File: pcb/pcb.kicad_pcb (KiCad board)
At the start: 2 copper layers, 46 x 58 mm, 39 parts, among them J1 USB_C_Receptacle_USB2.0_14P, J3 LCD DATA, J4 LCD CTRL, J5 MOISTURE, J6 HC-05, J7 DEBUG, J9 USART3 TX, SW1 PWR SWITCH, U1 TLV62569DBV, U2 STM32F446RETx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

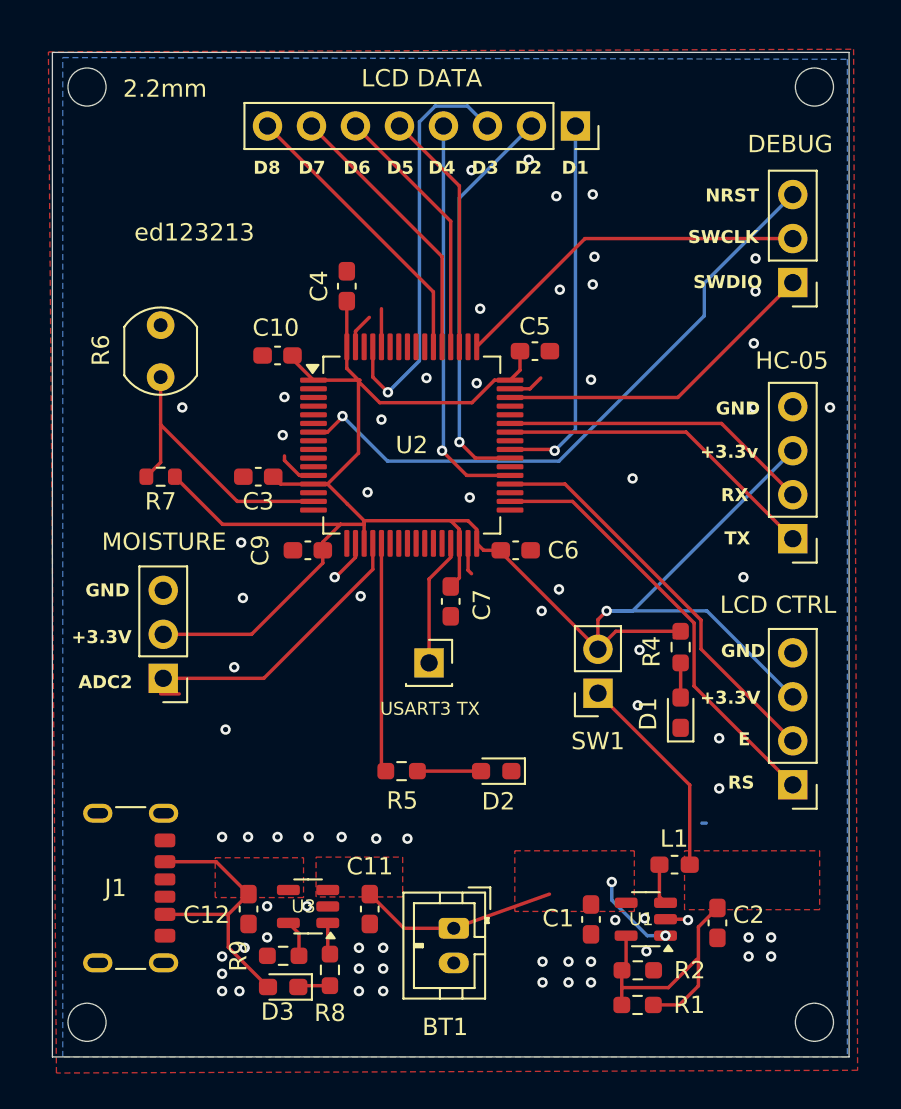
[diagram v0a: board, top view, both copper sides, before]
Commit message: add vcap capacitor and widen traces
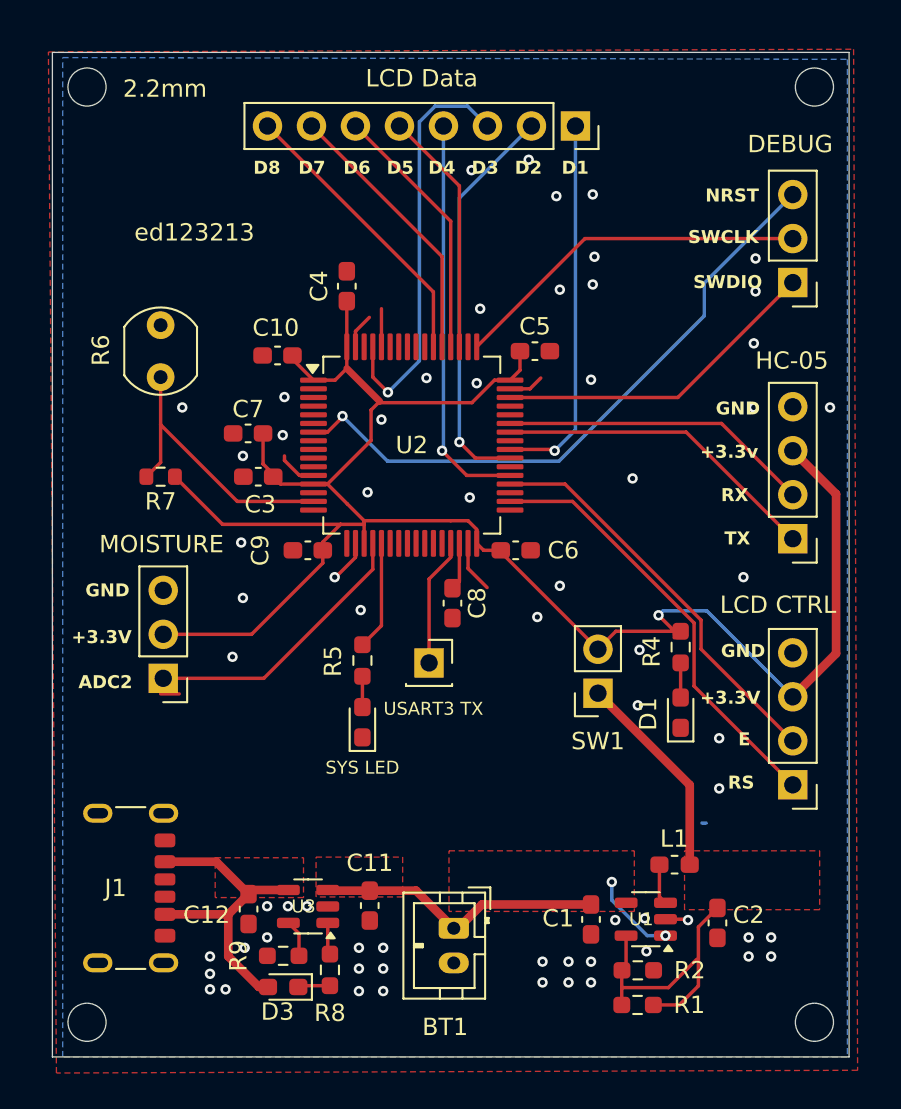
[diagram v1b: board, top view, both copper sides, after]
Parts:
- added C8: 4.7uF, Capacitor_SMD:C_0603_1608Metric_Pad1.08x0.95mm_HandSolder, F.Cu at (88.1, 72.3)
- J3: value LCD DATA -> LCD Data
- moved C7 15.2 mm to (76.3, 62.5), turned to 180 degrees
- moved D2 8.23 mm to (82.9, 79.2), turned to 90 degrees
- moved R5 6.78 mm to (82.9, 75.6), turned to 90 degrees
- moved C11 0.20 mm to (83.3, 89.8)
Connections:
- U2 pad 30: +3.3V -> Net-(U2-VCAP_1)
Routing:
- net +3.7V: track 10.7 -> 21.7 mm
- net SYS LED: track 13.3 -> 6.31 mm
- net +3.3V: track 147.5 -> 142.9 mm
- net Net-(U2-VCAP_1): track 0.00 -> 2.75 mm
- net +5V: track 16.1 -> 18.8 mm
- net Net-(D2-A): track 3.67 -> 1.77 mm
- net GND: track 14.8 -> 15.8 mm, vias 71 -> 65

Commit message: increase board outline
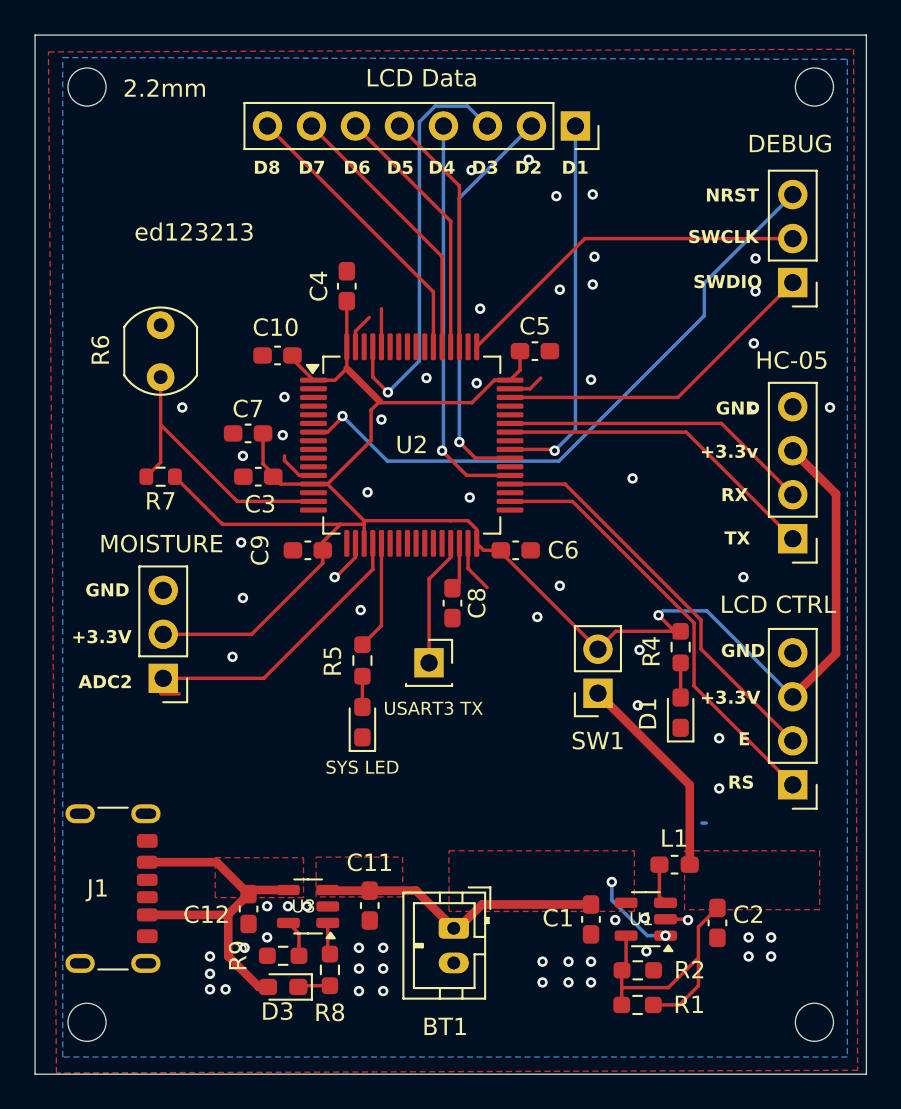
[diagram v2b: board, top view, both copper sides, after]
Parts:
- moved J1 1.02 mm to (67.4, 88.8)
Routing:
- net +5V: track 18.8 -> 22.5 mm
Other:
- board size 46 x 58 mm -> 48 x 60 mm
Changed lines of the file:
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@@
 			(usegerberattributes yes)
 			(usegerberadvancedattributes yes)
-			(creategerberjobfile yes)
+			(creategerberjobfile no)
 			(dashed_line_dash_ratio 12.000000)
 			(dashed_line_gap_ratio 3.000000)
@@
 			(drillshape 0)
 			(scaleselection 1)
-			(outputdirectory "gerber/")
+			(outputdirectory "gerber/drill/")
 		)
 	)
@@
 	(footprint "Connector_USB:USB_C_Receptacle_GCT_USB4125-xx-x-0190_6P_TopMnt_Horizontal"
 		(layer "F.Cu")
-		(at 68.42 88.75 -90)
+		(at 67.4 88.78 -90)
 		(descr "USB Type C Receptacle, GCT, power-only, 6P, top mounted, horizontal, 3A, 1.9mm stake: https://gct.co/files/drawings/usb4125.pdf")
 		(tags "USB C Type-C receptacle power-only charging-only 6P 6C right angled")
@@
 	)
 	(gr_rect
-		(start 65 40.5)
-		(end 111 98.5)
+		(start 64 39.5)
+		(end 112 99.5)
 		(stroke
 			(width 0.05)
@@
 	)
 	(segment
-		(start 75.155 90.27)
-		(end 75.155 92.6925)
+		(start 75.125 90.3)
+		(end 76.325 89.1)
+		(width 0.2)
+		(layer "F.Cu")
+		(net 5)
+	)
+	(segment
+		(start 76.325 89.1)
+		(end 74.485 87.26)
 		(width 0.5)
 		(layer "F.Cu")
@@
 	)
 	(segment
-		(start 78.625 88.8625)
-		(end 76.5625 88.8625)
+		(start 74.485 87.26)
+		(end 70.48 87.26)
 		(width 0.5)
 		(layer "F.Cu")
@@
 	)
 	(segment
-		(start 71.5 90.27)
-		(end 75.155 90.27)
+		(start 75.155 90.27)
+		(end 75.155 92.6925)
 		(width 0.5)
 		(layer "F.Cu")
@@
 	)
 	(segment
-		(start 76.925 94.4625)
-		(end 77.45 94.4625)
+		(start 78.625 88.8625)
+		(end 76.5625 88.8625)
 		(width 0.5)
 		(layer "F.Cu")
@@
 	)
 	(segment
-		(start 75.155 90.27)
-		(end 76.325 89.1)
+		(start 76.925 94.4625)
+		(end 77.45 94.4625)
 		(width 0.5)
 		(layer "F.Cu")
@@
 	)
 	(segment
-		(start 71.5 87.23)
-		(end 74.455 87.23)
+		(start 75.155 90.27)
+		(end 76.325 89.1)
 		(width 0.5)
 		(layer "F.Cu")
@@
 	)
 	(segment
-		(start 74.455 87.23)
-		(end 76.325 89.1)
+		(start 70.48 90.3)
+		(end 75.125 90.3)
 		(width 0.5)
 		(layer "F.Cu")

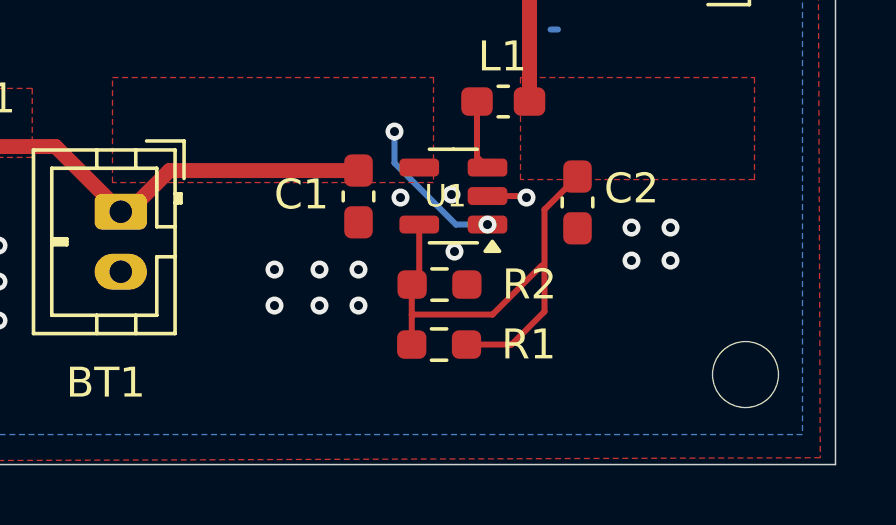
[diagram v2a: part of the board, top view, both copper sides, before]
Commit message: change design to use 0402 for buck converter
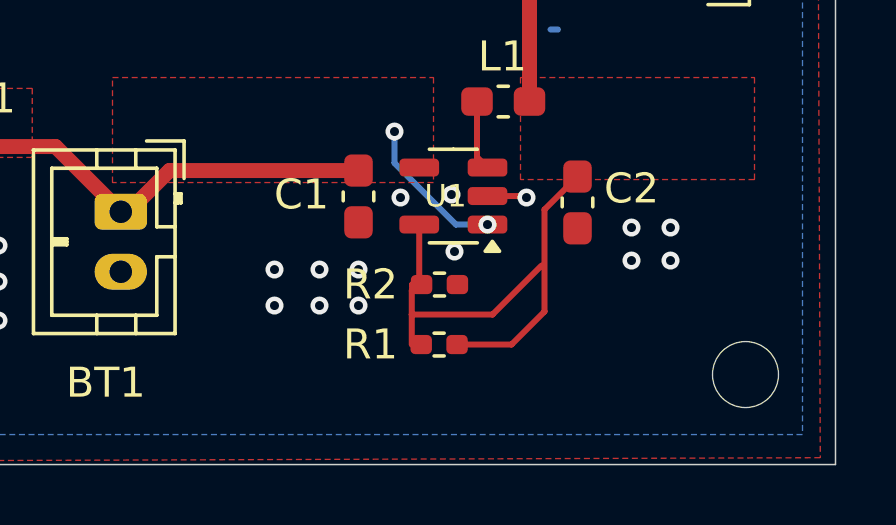
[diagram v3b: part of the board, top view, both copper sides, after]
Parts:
- R1: value 900k -> 450k; footprint Resistor_SMD:R_0603_1608Metric_Pad0.98x0.95mm_HandSolder -> Resistor_SMD:R_0402_1005Metric_Pad0.72x0.64mm_HandSolder
- R2: value 200k -> 100k; footprint Resistor_SMD:R_0603_1608Metric_Pad0.98x0.95mm_HandSolder -> Resistor_SMD:R_0402_1005Metric_Pad0.72x0.64mm_HandSolder
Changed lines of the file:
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@@
 		)
 	)
-	(footprint "Resistor_SMD:R_0603_1608Metric_Pad0.98x0.95mm_HandSolder"
+	(footprint "Resistor_SMD:R_0402_1005Metric_Pad0.72x0.64mm_HandSolder"
 		(layer "F.Cu")
 		(at 98.7875 95.5 180)
-		(descr "Resistor SMD 0603 (1608 Metric), square (rectangular) end terminal, IPC-7351 nominal with elongated pad for handsoldering. (Body size source: IPC-SM-782 page 72, https://www.pcb-3d.com/wordpress/wp-content/uploads/ipc-sm-782a_amendment_1_and_2.pdf), generated with kicad-footprint-generator")
+		(descr "Resistor SMD 0402 (1005 Metric), square (rectangular) end terminal, IPC-7351 nominal with elongated pad for handsoldering. (Body size source: IPC-SM-782 page 72, https://www.pcb-3d.com/wordpress/wp-content/uploads/ipc-sm-782a_amendment_1_and_2.pdf), generated with kicad-footprint-generator")
 		(tags "resistor handsolder")
 		(property "Reference" "R1"
-			(at -2.9875 0 0)
+			(at 2.2875 0 180)
 			(layer "F.SilkS")
 			(effects
@@
 			)
 		)
-		(property "Value" "900k"
-			(at 0 1.43 0)
+		(property "Value" "450k"
+			(at 0 1.17 180)
 			(layer "F.Fab")
 			(effects
@@
 		)
 		(property "Datasheet" ""
-			(at 0 0 0)
+			(at 0 0 180)
 			(layer "F.Fab")
 			(hide yes)
@@
 		)
 		(property "Description" "Resistor, small symbol"
-			(at 0 0 0)
+			(at 0 0 180)
 			(layer "F.Fab")
 			(hide yes)
@@
 		(attr smd)
 		(fp_line
-			(start -0.254724 0.5225)
-			(end 0.254724 0.5225)
+			(start -0.167621 0.38)
+			(end 0.167621 0.38)
 			(stroke
 				(width 0.12)
@@
 		)
 		(fp_line
-			(start -0.254724 -0.5225)
-			(end 0.254724 -0.5225)
+			(start -0.167621 -0.38)
+			(end 0.167621 -0.38)
 			(stroke
 				(width 0.12)
@@
 		)
 		(fp_line
-			(start 1.65 0.73)
-			(end -1.65 0.73)
+			(start 1.11 0.47)
+			(end -1.11 0.47)
 			(stroke
 				(width 0.05)
@@
 		)
 		(fp_line
-			(start 1.65 -0.73)
-			(end 1.65 0.73)
+			(start 1.11 -0.47)
+			(end 1.11 0.47)
 			(stroke
 				(width 0.05)
@@
 		)
 		(fp_line
-			(start -1.65 0.73)
-			(end -1.65 -0.73)
+			(start -1.11 0.47)
+			(end -1.11 -0.47)
 			(stroke
 				(width 0.05)
@@
 		)
 		(fp_line
-			(start -1.65 -0.73)
-			(end 1.65 -0.73)
+			(start -1.11 -0.47)
+			(end 1.11 -0.47)
 			(stroke
 				(width 0.05)
@@
 		)
 		(fp_line
-			(start 0.8 0.4125)
-			(end -0.8 0.4125)
+			(start 0.525 0.27)
+			(end -0.525 0.27)
 			(stroke
 				(width 0.1)
@@
 		)
 		(fp_line
-			(start 0.8 -0.4125)
-			(end 0.8 0.4125)
+			(start 0.525 -0.27)
+			(end 0.525 0.27)
 			(stroke
 				(width 0.1)
@@
 		)
 		(fp_line
-			(start -0.8 0.4125)
-			(end -0.8 -0.4125)
+			(start -0.525 0.27)
+			(end -0.525 -0.27)
 			(stroke
 				(width 0.1)
@@
 		)
 		(fp_line
-			(start -0.8 -0.4125)
-			(end 0.8 -0.4125)
+			(start -0.525 -0.27)
+			(end 0.525 -0.27)
 			(stroke
 				(width 0.1)
@@
 		)
 		(fp_text user "${REFERENCE}"
-			(at 0 0 0)
+			(at 0 0 180)
 			(layer "F.Fab")
 			(effects
 				(font
-					(size 0.4 0.4)
-					(thickness 0.06)
+					(size 0.26 0.26)
+					(thickness 0.04)
 				)
 			)
 		)
 		(pad "1" smd roundrect
-			(at -0.9125 0 180)
-			(size 0.975 0.95)
+			(at -0.5975 0 180)
+			(size 0.715 0.64)
 			(layers "F.Cu" "F.Mask" "F.Paste")
 			(roundrect_rratio 0.25)
@@
 		)
 		(pad "2" smd roundrect
-			(at 0.9125 0 180)
-			(size 0.975 0.95)
+			(at 0.5975 0 180)
+			(size 0.715 0.64)
 			(layers "F.Cu" "F.Mask" "F.Paste")
 			(roundrect_rratio 0.25)
@@
 		)
 		(embedded_fonts no)
-		(model "${KICAD9_3DMODEL_DIR}/Resistor_SMD.3dshapes/R_0603_1608Metric.step"
+		(model "${KICAD9_3DMODEL_DIR}/Resistor_SMD.3dshapes/R_0402_1005Metric.step"
 			(offset
 				(xyz 0 0 0)
@@
 		(embedded_fonts no)
 	)
-	(footprint "Resistor_SMD:R_0603_1608Metric_Pad0.98x0.95mm_HandSolder"
+	(footprint "Resistor_SMD:R_0402_1005Metric_Pad0.72x0.64mm_HandSolder"
 		(layer "F.Cu")
 		(at 98.8 93.5)
-		(descr "Resistor SMD 0603 (1608 Metric), square (rectangular) end terminal, IPC-7351 nominal with elongated pad for handsoldering. (Body size source: IPC-SM-782 page 72, https://www.pcb-3d.com/wordpress/wp-content/uploads/ipc-sm-782a_amendment_1_and_2.pdf), generated with kicad-footprint-generator")
+		(descr "Resistor SMD 0402 (1005 Metric), square (rectangular) end terminal, IPC-7351 nominal with elongated pad for handsoldering. (Body size source: IPC-SM-782 page 72, https://www.pcb-3d.com/wordpress/wp-content/uploads/ipc-sm-782a_amendment_1_and_2.pdf), generated with kicad-footprint-generator")
 		(tags "resistor handsolder")
 		(property "Reference" "R2"
-			(at 3 0 0)
+			(at -2.3 0 0)
 			(layer "F.SilkS")
 			(effects
@@
 			)
 		)
-		(property "Value" "200k"
-			(at 0 1.43 0)
+		(property "Value" "100k"
+			(at 0 1.17 0)
 			(layer "F.Fab")
 			(effects
@@
 		(attr smd)
 		(fp_line
-			(start -0.254724 -0.5225)
-			(end 0.254724 -0.5225)
+			(start -0.167621 -0.38)
+			(end 0.167621 -0.38)
 			(stroke
 				(width 0.12)
@@
 		)
 		(fp_line
-			(start -0.254724 0.5225)
-			(end 0.254724 0.5225)
+			(start -0.167621 0.38)
+			(end 0.167621 0.38)
 			(stroke
 				(width 0.12)
@@
 		)
 		(fp_line
-			(start -1.65 -0.73)
-			(end 1.65 -0.73)
+			(start -1.11 -0.47)
+			(end 1.11 -0.47)
 			(stroke
 				(width 0.05)
@@
 		)
 		(fp_line
-			(start -1.65 0.73)
-			(end -1.65 -0.73)
+			(start -1.11 0.47)
+			(end -1.11 -0.47)
 			(stroke
 				(width 0.05)
@@
 		)
 		(fp_line
-			(start 1.65 -0.73)
-			(end 1.65 0.73)
+			(start 1.11 -0.47)
+			(end 1.11 0.47)
 			(stroke
 				(width 0.05)
@@
 		)
 		(fp_line
-			(start 1.65 0.73)
-			(end -1.65 0.73)
+			(start 1.11 0.47)
+			(end -1.11 0.47)
 			(stroke
 				(width 0.05)
@@
 		)
 		(fp_line
-			(start -0.8 -0.4125)
-			(end 0.8 -0.4125)
+			(start -0.525 -0.27)
+			(end 0.525 -0.27)
 			(stroke
 				(width 0.1)
@@
 		)
 		(fp_line
-			(start -0.8 0.4125)
-			(end -0.8 -0.4125)
+			(start -0.525 0.27)
+			(end -0.525 -0.27)
 			(stroke
 				(width 0.1)
@@
 		)
 		(fp_line
-			(start 0.8 -0.4125)
-			(end 0.8 0.4125)
+			(start 0.525 -0.27)
+			(end 0.525 0.27)
 			(stroke
 				(width 0.1)
@@
 		)
 		(fp_line
-			(start 0.8 0.4125)
-			(end -0.8 0.4125)
+			(start 0.525 0.27)
+			(end -0.525 0.27)
 			(stroke
 				(width 0.1)
@@
 			(effects
 				(font
-					(size 0.4 0.4)
-					(thickness 0.06)
+					(size 0.26 0.26)
+					(thickness 0.04)
 				)
 			)
 		)
 		(pad "1" smd roundrect
-			(at -0.9125 0)
-			(size 0.975 0.95)
+			(at -0.5975 0)
+			(size 0.715 0.64)
 			(layers "F.Cu" "F.Mask" "F.Paste")
 			(roundrect_rratio 0.25)
@@
 		)
 		(pad "2" smd roundrect
-			(at 0.9125 0)
-			(size 0.975 0.95)
+			(at 0.5975 0)
+			(size 0.715 0.64)
 			(layers "F.Cu" "F.Mask" "F.Paste")
 			(roundrect_rratio 0.25)
@@
 		)
 		(embedded_fonts no)
-		(model "${KICAD9_3DMODEL_DIR}/Resistor_SMD.3dshapes/R_0603_1608Metric.step"
+		(model "${KICAD9_3DMODEL_DIR}/Resistor_SMD.3dshapes/R_0402_1005Metric.step"
 			(offset
 				(xyz 0 0 0)
